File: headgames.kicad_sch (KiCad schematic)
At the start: 38 parts, among them J1 ELECTRODES, U1 LM324N, U2 LM386

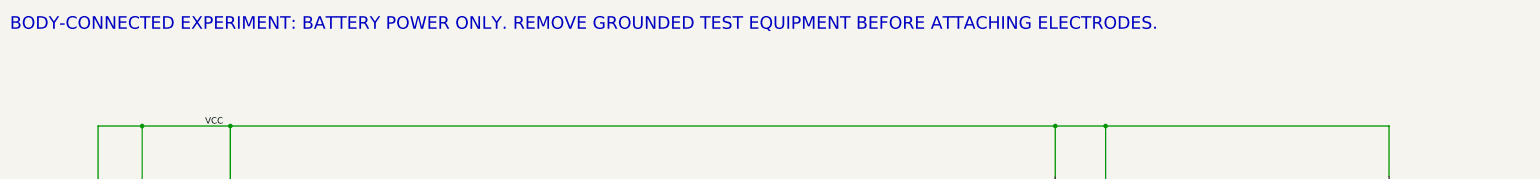
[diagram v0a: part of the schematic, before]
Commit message: Document the board as externally wired
Remove all tracked references to battery or AA-cell operation from the authoritative schematic, project guidance, README, and build-now visual. Rename the illustrated supply rail consistently to VCC and depict the source as an isolated wired 9 V DC input.

Retain the body-connected safety invariant in terms appropriate to a wired board: the external DC supply must remain isolated from mains earth and USB while electrodes are attached, and grounded or non-isolated equipment must be disconnected.

Verification: python3 manage.py test; xmllint --noout BUILD_NOW.svg; git grep confirms no battery, BAT+, or AA terminology remains in tracked sources; kicad-cli successfully parses the schematic for ERC. The two existing undriven-power ERC findings remain unchanged and are outside this terminology checkpoint.
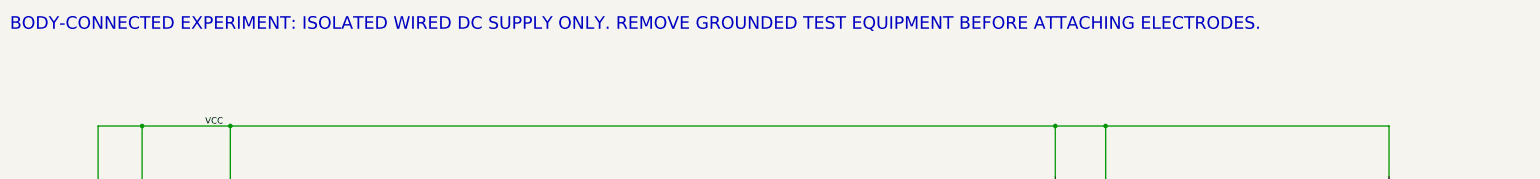
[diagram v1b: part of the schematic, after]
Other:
- note added: "BODY-CONNECTED EXPERIMENT: ISOLATED WIRED DC SUPPLY ONLY. REMOVE GROUNDED TEST EQUIPMENT BEFORE ATTACHING ELECTRODES."
- note removed: "BODY-CONNECTED EXPERIMENT: BATTERY POWER ONLY. REMOVE GROUNDED TEST EQUIPMENT BEFORE ATTACHING ELECTRODES."
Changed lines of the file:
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@@
 		(rev "A")
 		(company "Headgames")
-		(comment 1 "BATTERY ONLY WHILE ELECTRODES ARE CONNECTED")
+		(comment 1 "ISOLATED WIRED DC SUPPLY ONLY WHILE ELECTRODES ARE CONNECTED")
 		(comment 2 "LM324 reference and carrier into LM386 speaker amplifier")
 		(comment 3 "Pins 1 and 8 of LM386 intentionally open for gain 20")
@@
 		)
 	)
-	(text "BODY-CONNECTED EXPERIMENT: BATTERY POWER ONLY. REMOVE GROUNDED TEST EQUIPMENT BEFORE ATTACHING ELECTRODES."
+	(text "BODY-CONNECTED EXPERIMENT: ISOLATED WIRED DC SUPPLY ONLY. REMOVE GROUNDED TEST EQUIPMENT BEFORE ATTACHING ELECTRODES."
 		(exclude_from_sim no)
 		(at 17.78 19.05 0)

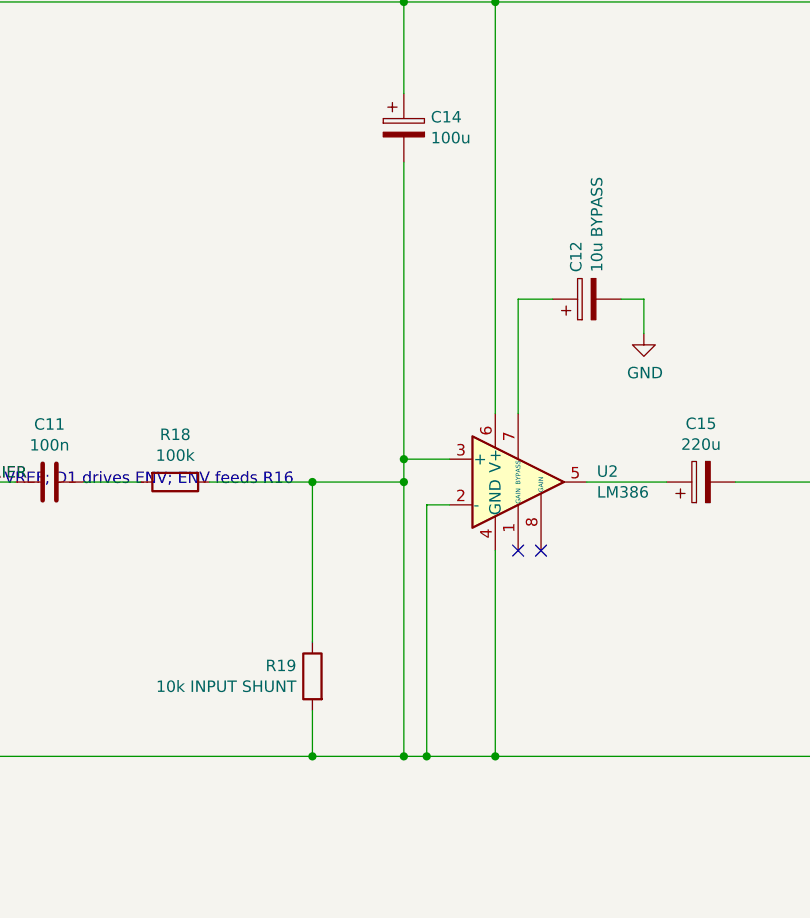
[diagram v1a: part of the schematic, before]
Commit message: Fix LM386 carrier input connectivity
Remove the unintended ground leg from the attenuated carrier node so the C11/R18 signal path reaches LM386 pin 3. Preserve the intended R19 input shunt and grounded inverting input, while giving C14 an independent local ground symbol so supply decoupling no longer relies on the faulty shared wire.

Replace the placeholder project test with a KiCad-netlist connectivity check. The root manage.py entrypoint now verifies that R18 and R19 meet U2 pin 3, that U2 pin 2 remains grounded, that pin 3 is not grounded, and that C14 still returns to ground. Temporary verification artifacts are created and removed within the project directory.

Verified with python3 manage.py test, kicad-cli ERC, Python bytecode compilation, and git diff --check. ERC retains the two existing externally-driven-power-net findings and introduces no audio-path violation.
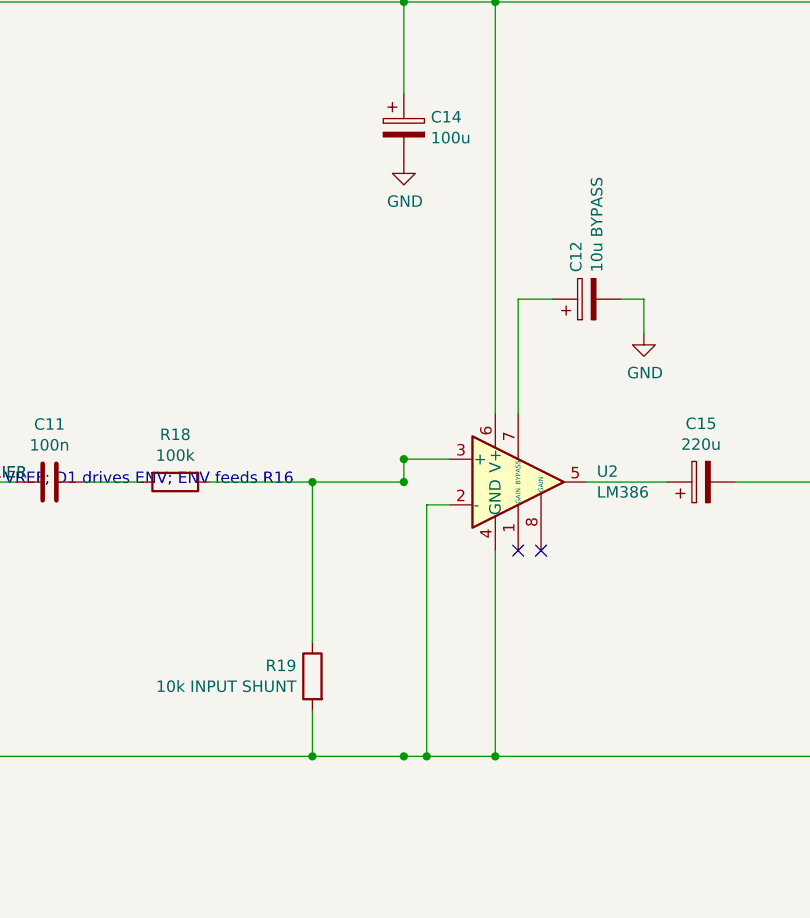
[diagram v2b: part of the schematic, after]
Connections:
- net GND: no longer R18.1, R19.1, U2.3 (+)
- new net: R18.1, R19.1, U2.3 (+)
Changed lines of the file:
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@@
-	(wire
-		(pts
-			(xy 228.6 91.44) (xy 228.6 121.92)
-		)
-		(stroke
-			(width 0)
-			(type default)
-		)
-	)
 	(wire
 		(pts
@@
 		(pts
 			(xy 125.73 200.66) (xy 119.38 200.66)
-		)
-		(stroke
-			(width 0)
-			(type default)
-		)
-	)
-	(wire
-		(pts
-			(xy 228.6 55.88) (xy 228.6 88.9)
 		)
 		(stroke
@@
 					(unit 1)
 				)
+			)
+		)
+	)
+	(symbol
+		(lib_id "power:GND")
+		(at 228.6 55.88 0)
+		(unit 1)
+		(exclude_from_sim no)
+		(in_bom yes)
+		(on_board yes)
+		(dnp no)
+		(property "Reference" "#PWR0103"
+			(at 228.6 62.23 0)
+			(effects
+				(font
+					(size 1.27 1.27)
+				)
+				(hide yes)
+			)
+		)
+		(property "Value" "GND"
+			(at 228.727 60.2742 0)
+			(effects
+				(font
+					(size 1.27 1.27)
+				)
+			)
+		)
+		(property "Footprint" ""
+			(at 228.6 55.88 0)
+			(effects
+				(font
+					(size 1.27 1.27)
+				)
+			)
+		)
+		(property "Datasheet" ""
+			(at 228.6 55.88 0)
+			(effects
+				(font
+					(size 1.27 1.27)
+				)
+			)
+		)
+		(property "Description" ""
+			(at 228.6 55.88 0)
+			(effects
+				(font
+					(size 1.27 1.27)
+				)
+			)
+		)
+		(pin "1"
+		)
+		(instances
+			(project "headgames"
+				(path "/16bca6b0-2f64-4676-a185-d512cb0de7e5"
+					(reference "#PWR0103")
+					(unit 1)
+				)

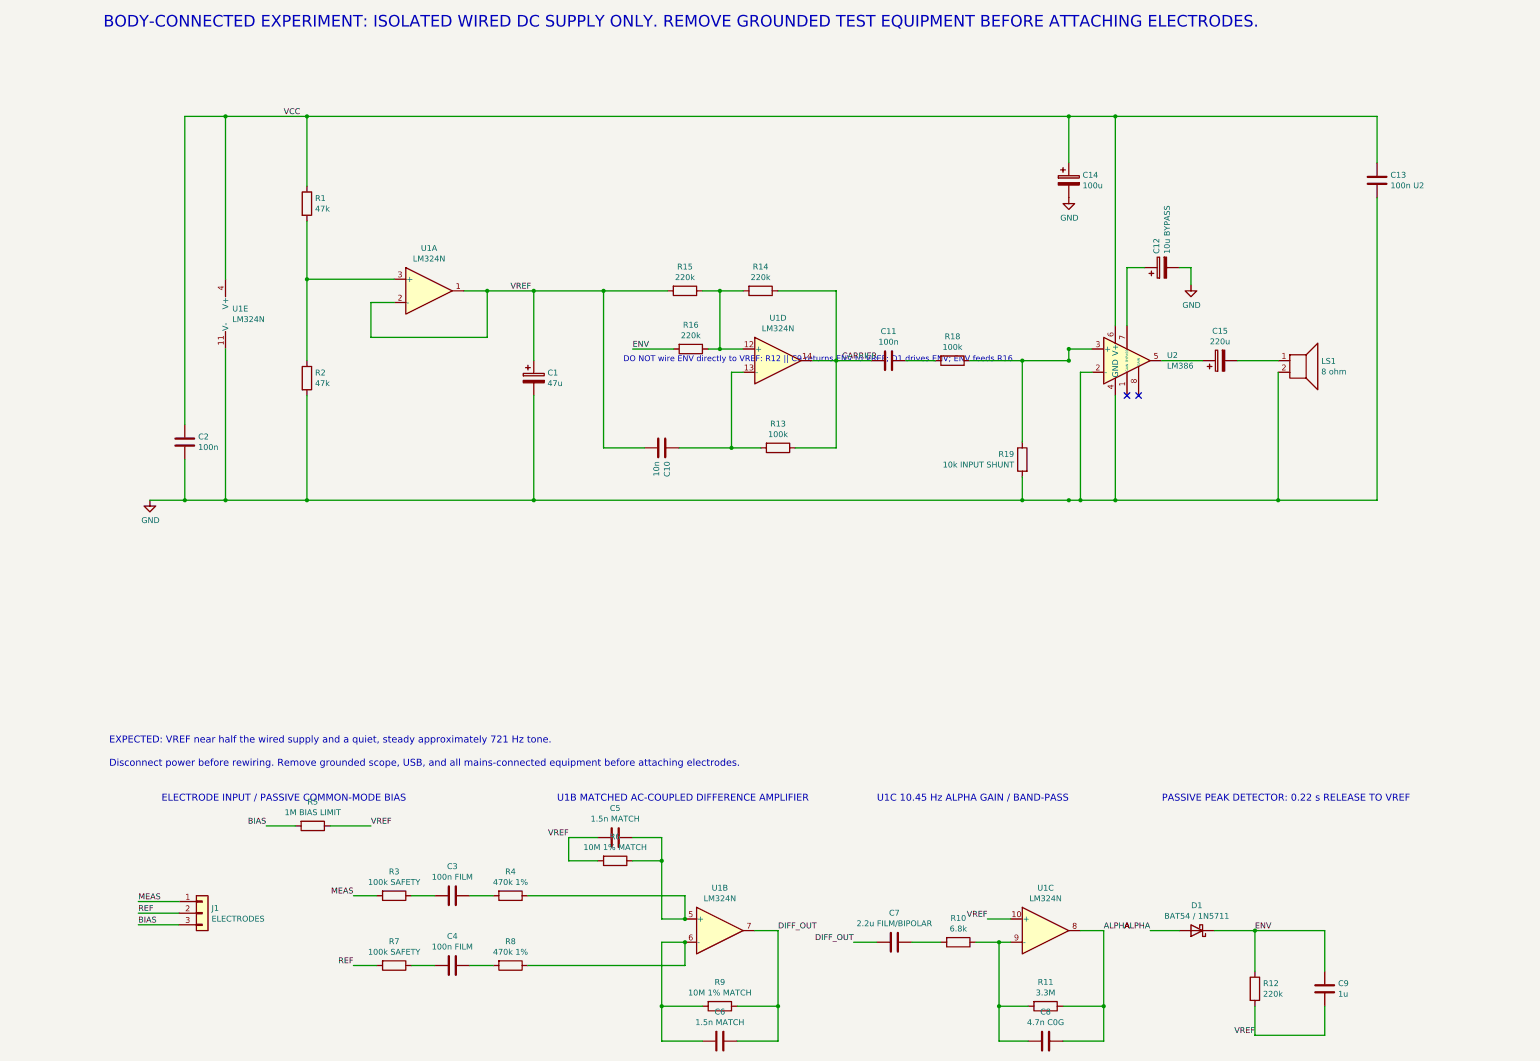
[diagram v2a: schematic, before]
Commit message: Restore LM386 input path after schematic relayout
Accept the newly saved authoritative KiCad layout while restoring the carrier-to-audio connectivity invariant lost during the overwrite. Remove the ground leg that shorted the R18/R19/U2 pin 3 node, leaving R19 as the intended input shunt and U2 pin 2 as the grounded inverting input.

Separate C14 supply decoupling from the signal path by returning its negative terminal through a dedicated GND symbol. This prevents the bulk-decoupling connection from recreating a conductive short between the LM386 non-inverting input and ground.

Verified the current schematic with python3 manage.py test, a direct kicad-cli netlist export, kicad-cli ERC, Python bytecode compilation, and git diff --check. The exported netlist places R18 pin 1, R19 pin 1, and U2 pin 3 together while C14 pin 2, R19 pin 2, and U2 pins 2/4 remain on GND. ERC retains only the two expected externally driven power-net reports.
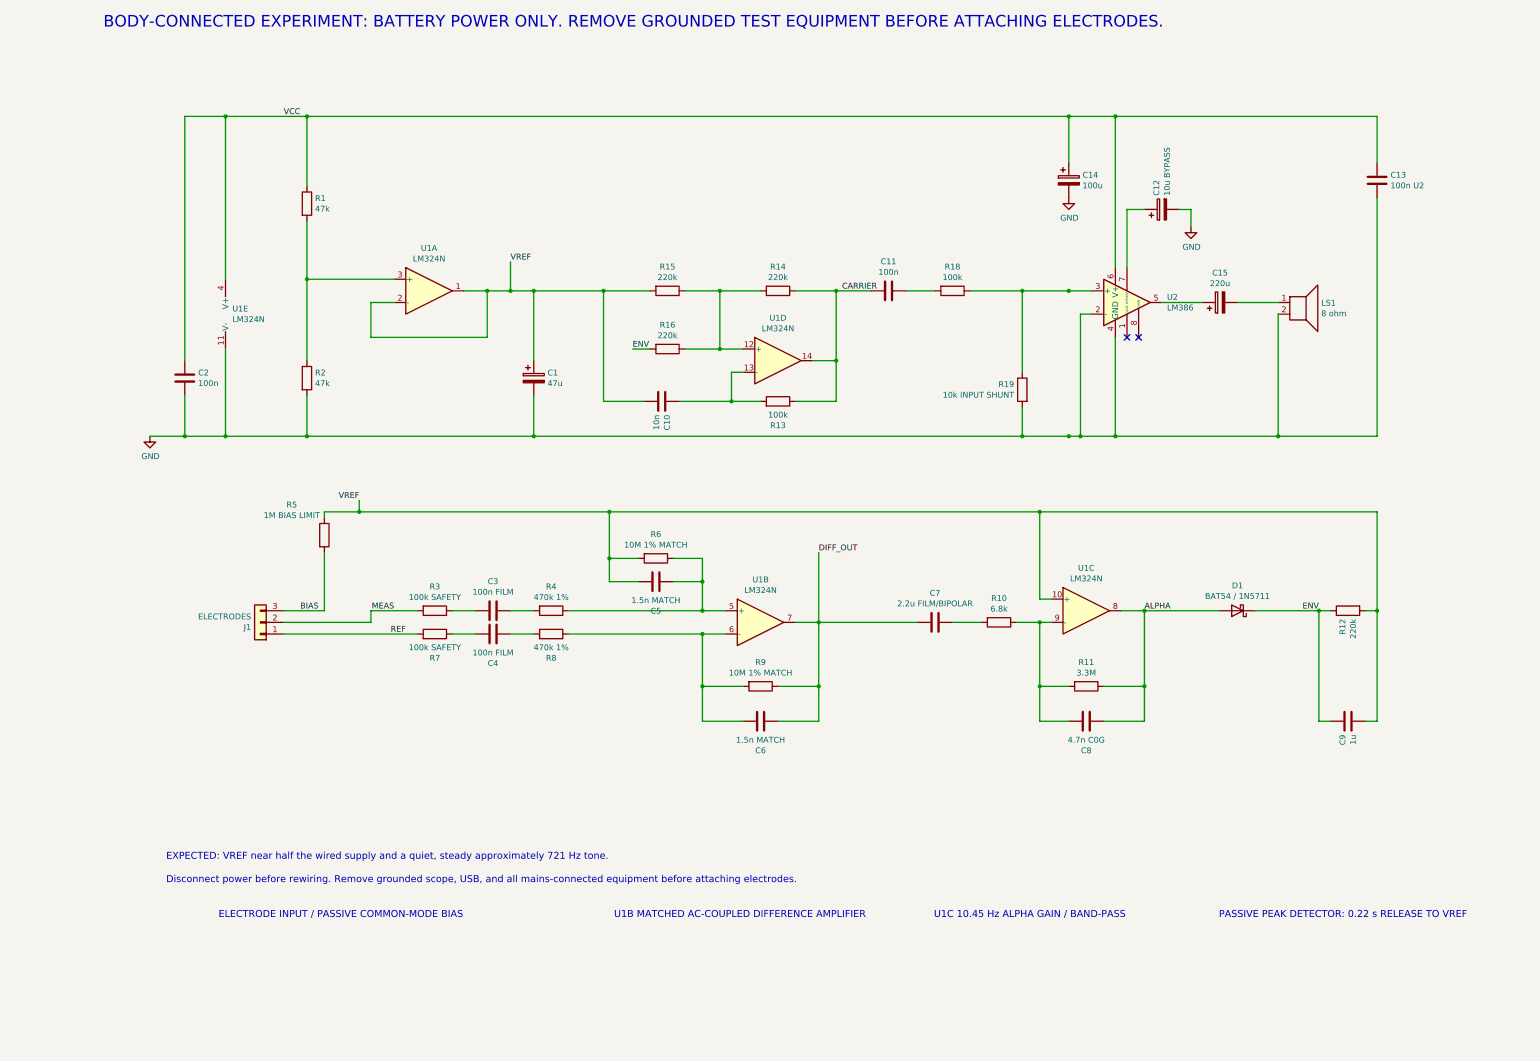
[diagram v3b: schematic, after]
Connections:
- net MEAS: now also J1.2 (Pin_2); no longer J1.1 (Pin_1)
- net REF: now also J1.1 (Pin_1); no longer J1.2 (Pin_2)
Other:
- note added: "BODY-CONNECTED EXPERIMENT: BATTERY POWER ONLY. REMOVE GROUNDED TEST EQUIPMENT BEFORE ATTACHING ELECTRODES."
- note removed: "BODY-CONNECTED EXPERIMENT: ISOLATED WIRED DC SUPPLY ONLY. REMOVE GROUNDED TEST EQUIPMENT BEFORE ATTACHING ELECTRODES."
- note removed: "DO NOT wire ENV directly to VREF: R12 || C9 returns ENV to VREF; D1 drives ENV; ENV feeds R16"
- moved on the sheet: C10, C11, C12, C15, C2, C3, C4, C5, C6, C7, C8, C9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

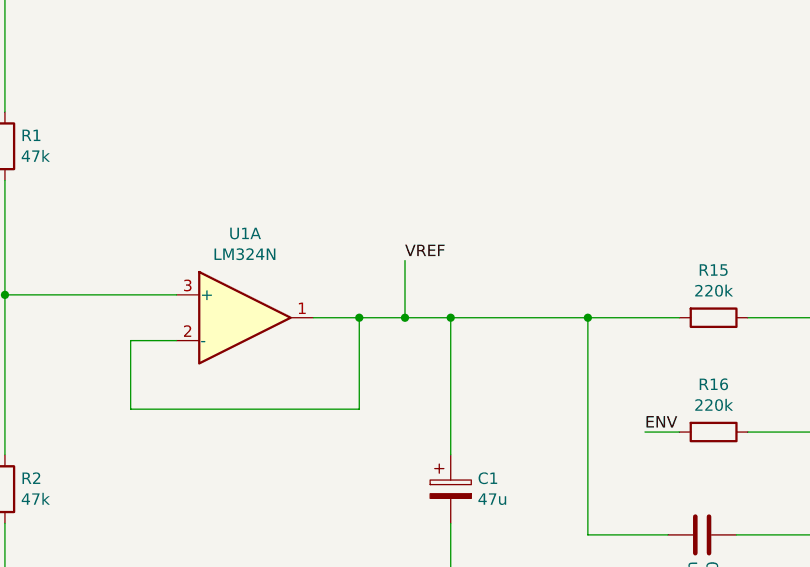
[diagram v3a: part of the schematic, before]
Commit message: Isolate buffered VREF from reservoir capacitance
Insert R17 as a 100 ohm series isolation resistor between the U1A voltage-follower output and the distributed VREF rail. Keep U1A feedback connected on the amplifier side of R17 so the 47 uF C1 reservoir cannot sit inside the follower loop or directly load the LM324 output.

Extend the root manage.py connectivity verification to require the follower feedback topology, both sides of R17, and electrical separation between C1 and U1A's output. This turns the stability boundary into a durable schematic invariant.

Verified with 'uv run ./manage.py test', KiCad 9 netlist export through the test harness, and 'git diff --check'. KiCad ERC still reports only the two pre-existing undriven power-net errors.
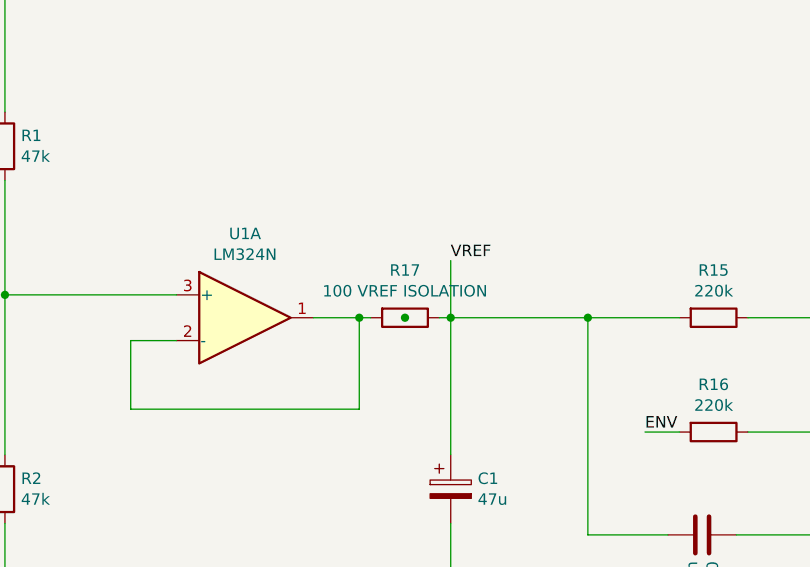
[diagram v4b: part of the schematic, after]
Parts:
- added R17: 100 VREF ISOLATION, symbol Device:R
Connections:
- net VREF: now also R17.1; no longer U1.1, U1.2 (-)
- new net: R17.2, U1.1, U1.2 (-)
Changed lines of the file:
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@@
 	(wire
 		(pts
-			(xy 101.6 76.2) (xy 106.68 76.2)
+			(xy 101.6 76.2) (xy 102.87 76.2)
 		)
 		(stroke
@@
 	(wire
 		(pts
-			(xy 106.68 76.2) (xy 111.76 76.2)
+			(xy 110.49 76.2) (xy 111.76 76.2)
 		)
 		(stroke
@@
 	(wire
 		(pts
-			(xy 106.68 69.85) (xy 106.68 76.2)
+			(xy 111.76 69.85) (xy 111.76 76.2)
 		)
 		(stroke
@@
 	)
 	(label "VREF"
-		(at 106.68 69.85 0)
+		(at 111.76 69.85 0)
 		(effects
 			(font
@@
 					(unit 1)
 				)
+			)
+		)
+	)
+	(symbol
+		(lib_id "Device:R")
+		(at 106.68 76.2 270)
+		(unit 1)
+		(exclude_from_sim no)
+		(in_bom yes)
+		(on_board yes)
+		(dnp no)
+		(property "Reference" "R17"
+			(at 106.68 70.9422 90)
+			(effects
+				(font
+					(size 1.27 1.27)
+				)
+			)
+		)
+		(property "Value" "100 VREF ISOLATION"
+			(at 106.68 73.2536 90)
+			(effects
+				(font
+					(size 1.27 1.27)
+				)
+			)
+		)
+		(property "Footprint" ""
+			(at 106.68 76.2 0)
+			(effects
+				(font
+					(size 1.27 1.27)
+				)
+			)
+		)
+		(property "Datasheet" ""
+			(at 106.68 76.2 0)
+			(effects
+				(font
+					(size 1.27 1.27)
+				)
+			)
+		)
+		(property "Description" ""
+			(at 106.68 76.2 0)
+			(effects
+				(font
+					(size 1.27 1.27)
+				)
+			)
+		)
+		(pin "1"
+		)
+		(pin "2"
+		)
+		(instances
+			(project "headgames"
+				(path "/16bca6b0-2f64-4676-a185-d512cb0de7e5"
+					(reference "R17")
+					(unit 1)
+				)

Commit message: Bound LM386 carrier drive below clipping demand
Increase R18 from 100 kohm to 1 Mohm while retaining the 10 kohm input shunt and AC coupling. With the LM386's specified 50 kohm input resistance included in parallel with R19, the gain-20 amplifier now requests approximately 0.165 V/V of speaker-output swing for each volt of carrier swing instead of exceeding the available battery rail.

Refactor schematic extraction to return component values together with connectivity, add compact resistor-value parsing, and calculate the complete source-divider-plus-LM386 gain in the root verification command. Fail verification if the ideal carrier-to-output demand exceeds 0.2 V/V so future value edits cannot silently restore the overdrive condition.

Verified with 'UV_CACHE_DIR=.uv-cache uv run ./manage.py test', KiCad 9 ERC, rendered schematic inspection, and 'git diff --check'. ERC remains limited to the two pre-existing undriven power-net errors.
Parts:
- R18: value 100k -> 1M ATTEN
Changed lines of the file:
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@@
 			)
 		)
-		(property "Value" "100k"
+		(property "Value" "1M ATTEN"
 			(at 203.2 73.2536 90)
 			(effects
